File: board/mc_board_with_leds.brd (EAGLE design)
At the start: 70.3 x 34.5 mm, 36 parts, among them IC1 TPS61070DDC, IC2 MEGA8-P, Q2 16MHz

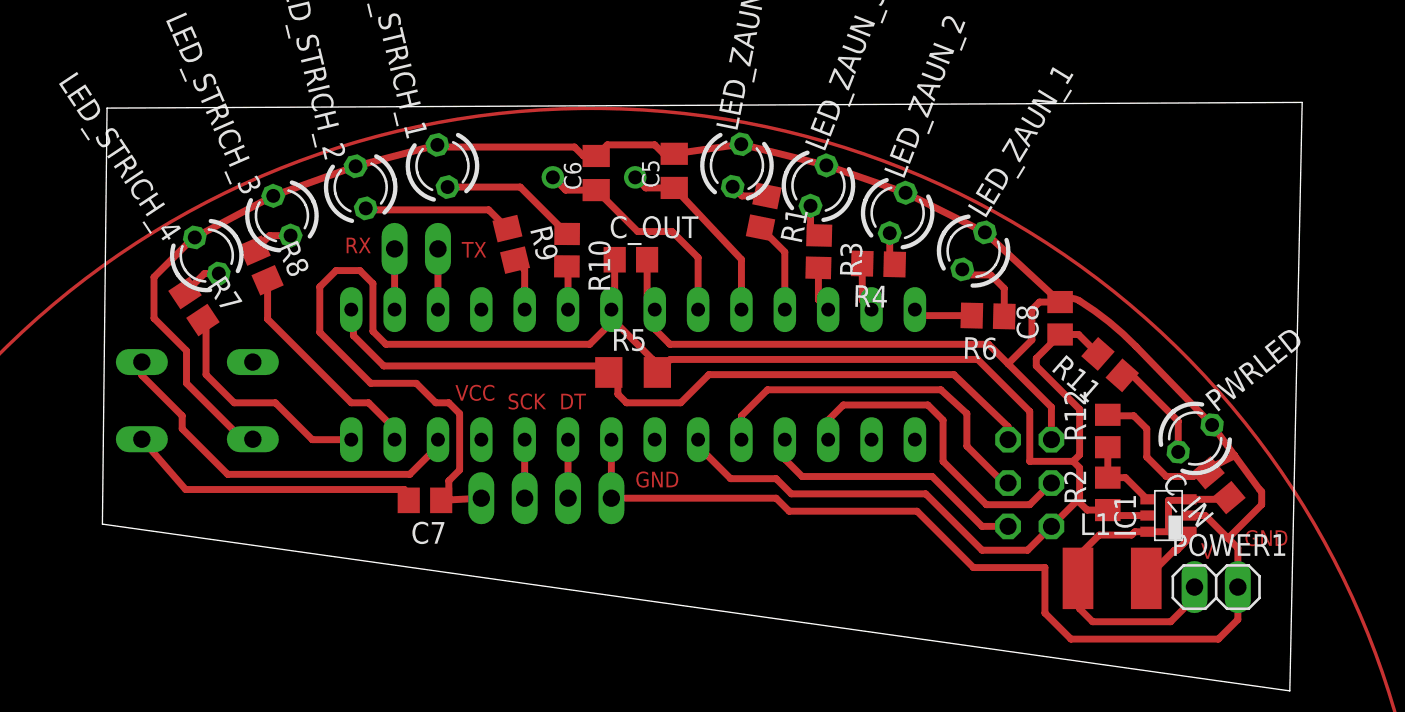
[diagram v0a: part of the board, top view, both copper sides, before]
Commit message: added drill holes
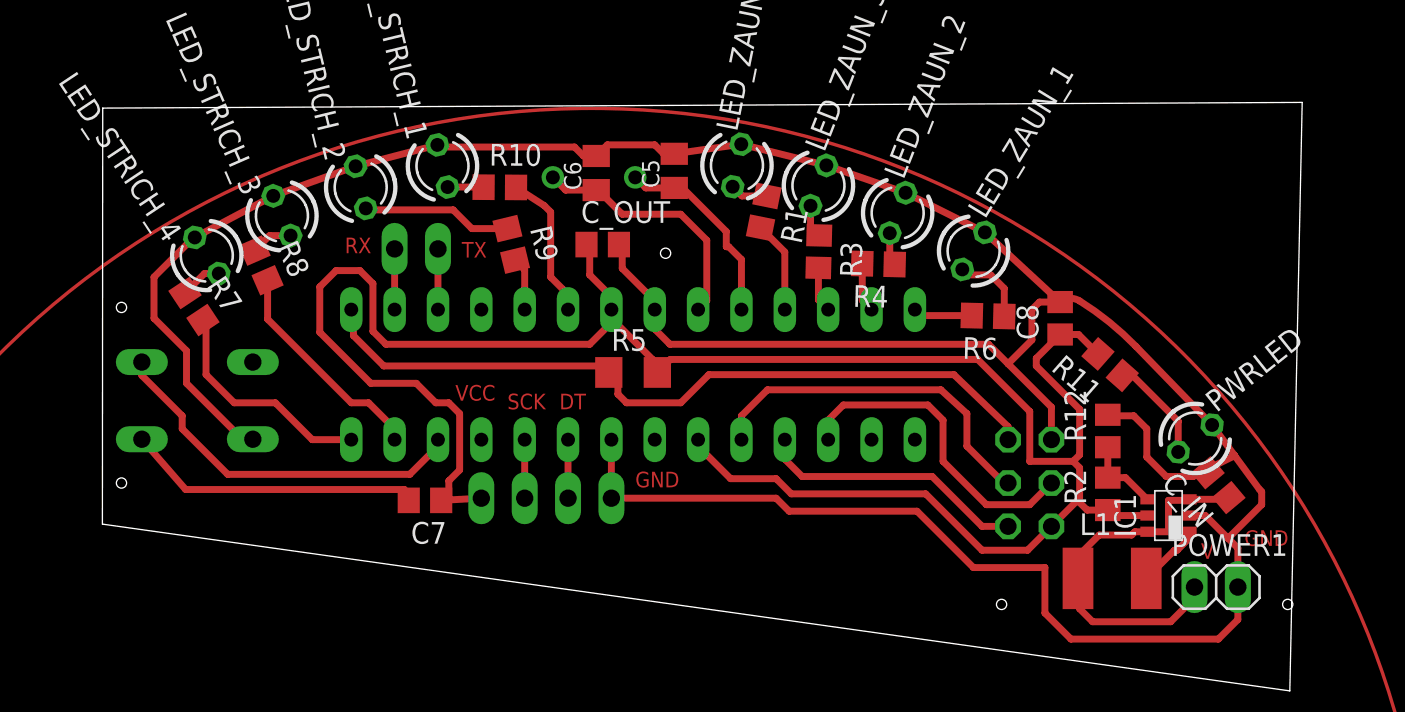
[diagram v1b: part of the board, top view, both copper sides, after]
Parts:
- moved R10 5.39 mm to (43.6, 44.4), turned to 359.6 degrees
- moved C_OUT 1.88 mm to (49.7, 41.0)
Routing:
- net PD4/LED_STRICH_1: track 2.56 -> 8.64 mm
- net N$12: track 8.14 -> 2.12 mm
- net GND: track 192.3 -> 193.9 mm
- net +5V: track 124.4 -> 125.8 mm
- net N$14: track 13.5 -> 14.8 mm
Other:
- outline, holes or cut-outs redrawn
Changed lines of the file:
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@@
 <layer number="43" name="vRestrict" color="2" fill="10" visible="no" active="yes"/>
 <layer number="44" name="Drills" color="7" fill="1" visible="no" active="yes"/>
-<layer number="45" name="Holes" color="7" fill="1" visible="no" active="yes"/>
+<layer number="45" name="Holes" color="7" fill="1" visible="yes" active="yes"/>
 <layer number="46" name="Milling" color="3" fill="1" visible="no" active="yes"/>
 <layer number="47" name="Measures" color="7" fill="1" visible="no" active="yes"/>
@@
 <board>
 <plain>
-<wire x1="20.345471875" y1="24.64364375" x2="20.617596875" y2="49.016115625" width="0" layer="20"/>
-<wire x1="20.617596875" y1="49.016115625" x2="90.63675" y2="49.349575" width="0" layer="20"/>
+<wire x1="20.345471875" y1="24.64364375" x2="20.363596875" y2="49.016115625" width="0" layer="20"/>
+<wire x1="20.363596875" y1="49.016115625" x2="90.63675" y2="49.349575" width="0" layer="20"/>
 <wire x1="90.63675" y1="49.349575" x2="89.912409375" y2="14.87245" width="0" layer="20"/>
 <wire x1="89.912409375" y1="14.87245" x2="20.345471875" y2="24.64364375" width="0" layer="20"/>
@@
 <text x="44.069" y="31.369" size="0.9144" layer="1" font="vector" ratio="28">SCK</text>
 <text x="41.021" y="31.877" size="0.9144" layer="1" font="vector" ratio="28">VCC</text>
+<hole x="21.463" y="37.338" drill="0.6"/>
+<hole x="89.789" y="19.939" drill="0.6"/>
+<hole x="73.025" y="19.939" drill="0.6"/>
+<hole x="21.463" y="27.051" drill="0.6"/>
+<hole x="53.34" y="40.513" drill="0.6"/>
 </plain>
 <attributes>
@@
 <element name="R8" library="resistor" package="R0805" value="470" x="29.6424875" y="39.798434375" rot="R293.6"/>
 <element name="R9" library="resistor" package="R0805" value="470" x="44.297534375" y="41.033296875" rot="R283.6"/>
-<element name="R10" library="resistor" package="R0805" value="470" x="47.565540625" y="40.692409375" rot="R269.6"/>
+<element name="R10" library="resistor" package="R0805" value="470" x="43.628540625" y="44.375409375" rot="R359.6"/>
 <element name="R11" library="resistor" package="R0805" value="470" x="79.383846875" y="33.986165625" rot="R138.6"/>
 <element name="PWRLED" library="led" package="LED3MM" value="" x="84.36773125" y="29.6607875" rot="R38.6"/>
@@
 <element name="R12" library="resistor" package="R0805" value="" x="79.248" y="30.099" rot="R90"/>
 <element name="C_IN" library="rcl-2" package="C0805" value="" x="85.725" y="26.924" rot="R130"/>
-<element name="C_OUT" library="rcl-2" package="C0805" value="" x="51.308" y="40.132"/>
+<element name="C_OUT" library="rcl-2" package="C0805" value="" x="49.657" y="41.021"/>
 </elements>
 <signals>
@@
 <wire x1="62.759478125" y1="45.658896875" x2="67.3998625" y2="44.054896875" width="0.4064" layer="1"/>
 <wire x1="67.3998625" y1="44.054896875" x2="72.04778125" y2="41.733921875" width="0.4064" layer="1"/>
-<wire x1="52.258" y1="40.132" x2="52.258" y2="37.658" width="0.4064" layer="1"/>
-<wire x1="52.258" y1="37.658" x2="52.705" y2="37.211" width="0.4064" layer="1"/>
 <wire x1="50.165" y1="26.162" x2="50.165" y2="29.591" width="0.4064" layer="1"/>
 <wire x1="76.454" y1="37.653" x2="72.04778125" y2="41.733921875" width="0.4064" layer="1"/>
@@
 <wire x1="88.265" y1="26.543" x2="88.265" y2="25.781" width="0.4064" layer="1"/>
 <wire x1="88.265" y1="25.781" x2="86.2965" y2="23.8125" width="0.4064" layer="1"/>
+<wire x1="52.705" y1="37.211" x2="52.705" y2="37.719" width="0.4064" layer="1"/>
+<wire x1="52.705" y1="37.719" x2="50.8" y2="39.624" width="0.4064" layer="1"/>
+<wire x1="50.8" y1="39.624" x2="50.8" y2="40.828" width="0.4064" layer="1"/>
+<wire x1="50.8" y1="40.828" x2="50.607" y2="41.021" width="0.4064" layer="1"/>
 </signal>
 <signal name="+5V">
@@
 <contactref element="R2" pad="1"/>
 <contactref element="C_OUT" pad="1"/>
-<wire x1="50.358" y1="40.132" x2="50.358" y2="37.404" width="0.4064" layer="1"/>
-<wire x1="50.358" y1="37.404" x2="50.165" y2="37.211" width="0.4064" layer="1"/>
 <wire x1="33.081" y1="38.542" x2="33.081" y2="35.88" width="0.4064" layer="1"/>
 <wire x1="33.081" y1="35.88" x2="36.068" y2="32.893" width="0.4064" layer="1"/>
@@
 <wire x1="52.578" y1="34.29" x2="52.578" y2="33.807" width="0.4064" layer="1"/>
 <wire x1="52.578" y1="33.807" x2="52.857" y2="33.528" width="0.4064" layer="1"/>
+<wire x1="50.165" y1="37.211" x2="50.165" y2="37.973" width="0.4064" layer="1"/>
+<wire x1="50.165" y1="37.973" x2="48.895" y2="39.243" width="0.4064" layer="1"/>
+<wire x1="48.895" y1="39.243" x2="48.895" y2="40.833" width="0.4064" layer="1"/>
+<wire x1="48.895" y1="40.833" x2="48.707" y2="41.021" width="0.4064" layer="1"/>
 </signal>
 <signal name="PB4/MISO">
@@
 <contactref element="IC2" pad="6"/>
 <contactref element="R10" pad="2"/>
-<wire x1="47.625" y1="37.211" x2="47.625" y2="39.6763375" width="0.4064" layer="1"/>
-<wire x1="47.625" y1="39.6763375" x2="47.55890625" y2="39.74243125" width="0.4064" layer="1" curve="90"/>
+<wire x1="44.578515625" y1="44.368775" x2="46.228" y2="43.307" width="0.4064" layer="1"/>
+<wire x1="47.625" y1="37.211" x2="47.371" y2="37.465" width="0.4064" layer="1"/>
+<wire x1="47.371" y1="37.465" x2="47.371" y2="38.354" width="0.4064" layer="1"/>
+<wire x1="47.371" y1="38.354" x2="46.609" y2="39.116" width="0.4064" layer="1"/>
+<wire x1="46.609" y1="39.116" x2="46.609" y2="42.926" width="0.4064" layer="1"/>
+<wire x1="46.609" y1="42.926" x2="46.228" y2="43.307" width="0.4064" layer="1"/>
 </signal>
 <signal name="PC0/DT">
@@
 <contactref element="LED_STRICH_2" pad="A"/>
 <wire x1="35.775934375" y1="43.140675" x2="35.863609375" y2="43.053" width="0.4064" layer="1"/>
-<wire x1="35.863609375" y1="43.053" x2="42.97780625" y2="43.053" width="0.4064" layer="1"/>
-<wire x1="44.074146875" y1="41.956659375" x2="42.97780625" y2="43.053" width="0.4064" layer="1"/>
+<wire x1="35.863609375" y1="43.053" x2="40.894" y2="43.053" width="0.4064" layer="1"/>
+<wire x1="40.894" y1="43.053" x2="41.990340625" y2="41.956659375" width="0.4064" layer="1"/>
+<wire x1="41.990340625" y1="41.956659375" x2="44.074146875" y2="41.956659375" width="0.4064" layer="1"/>
 </signal>
 <signal name="N$12">
 <contactref element="R10" pad="1"/>
 <contactref element="LED_STRICH_1" pad="A"/>
-<wire x1="47.572171875" y1="41.642384375" x2="44.8237125" y2="44.39084375" width="0.4064" layer="1"/>
-<wire x1="44.8237125" y1="44.39084375" x2="40.567609375" y2="44.39084375" width="0.4064" layer="1"/>
+<wire x1="40.567609375" y1="44.39084375" x2="42.6785625" y2="44.39084375" width="0.4064" layer="1"/>
+<wire x1="42.6785625" y1="44.39084375" x2="42.6785625" y2="44.382040625" width="0.4064" layer="1"/>
 </signal>
 <signal name="N$13">
@@
 <contactref element="IC2" pad="10"/>
 <wire x1="57.785" y1="37.211" x2="57.785" y2="40.148" width="0.4064" layer="1"/>
-<wire x1="57.785" y1="40.148" x2="53.848" y2="44.339" width="0.4064" layer="1"/>
 <wire x1="51.562" y1="44.958" x2="52.181" y2="44.339" width="0.4064" layer="1"/>
 <wire x1="52.181" y1="44.339" x2="53.848" y2="44.339" width="0.4064" layer="1"/>
+<wire x1="56.896" y1="40.894" x2="56.896" y2="41.783" width="0.4064" layer="1"/>
+<wire x1="56.896" y1="41.783" x2="54.34" y2="44.339" width="0.4064" layer="1"/>
+<wire x1="54.34" y1="44.339" x2="53.848" y2="44.339" width="0.4064" layer="1"/>
+<wire x1="57.785" y1="40.148" x2="57.039" y2="40.894" width="0.4064" layer="1"/>
+<wire x1="57.039" y1="40.894" x2="56.896" y2="40.894" width="0.4064" layer="1"/>
 </signal>
 <signal name="N$14">
@@
 <contactref element="Q2" pad="1"/>
 <contactref element="IC2" pad="9"/>
-<wire x1="51.705" y1="41.783" x2="53.721" y2="41.783" width="0.4064" layer="1"/>
-<wire x1="53.721" y1="41.783" x2="55.245" y2="40.259" width="0.4064" layer="1"/>
-<wire x1="55.245" y1="40.259" x2="55.245" y2="37.211" width="0.4064" layer="1"/>
 <wire x1="46.736" y1="44.958" x2="47.482" y2="44.212" width="0.4064" layer="1"/>
 <wire x1="47.482" y1="44.212" x2="49.276" y2="44.212" width="0.4064" layer="1"/>
-<wire x1="51.705" y1="41.783" x2="49.276" y2="44.212" width="0.4064" layer="1"/>
+<wire x1="55.245" y1="37.211" x2="55.753" y2="37.719" width="0.4064" layer="1"/>
+<wire x1="55.753" y1="37.719" x2="55.753" y2="41.275" width="0.4064" layer="1"/>
+<wire x1="55.753" y1="41.275" x2="54.229" y2="42.799" width="0.4064" layer="1"/>
+<wire x1="54.229" y1="42.799" x2="50.8" y2="42.799" width="0.4064" layer="1"/>
+<wire x1="50.8" y1="42.799" x2="49.387" y2="44.212" width="0.4064" layer="1"/>
+<wire x1="49.387" y1="44.212" x2="49.276" y2="44.212" width="0.4064" layer="1"/>
 </signal>
 <signal name="N$15">

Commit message: added ground fill
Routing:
- added copper zone on layer 1, net GND
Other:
- board size 70.3 x 34.5 mm -> 76.4 x 34.3 mm
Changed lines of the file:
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@@
 <board>
 <plain>
-<wire x1="20.345471875" y1="24.64364375" x2="20.363596875" y2="49.016115625" width="0" layer="20"/>
-<wire x1="20.363596875" y1="49.016115625" x2="90.63675" y2="49.349575" width="0" layer="20"/>
-<wire x1="90.63675" y1="49.349575" x2="89.912409375" y2="14.87245" width="0" layer="20"/>
-<wire x1="89.912409375" y1="14.87245" x2="20.345471875" y2="24.64364375" width="0" layer="20"/>
-<circle x="49" y="0" radius="49" width="0.2" layer="1"/>
+<wire x1="17.551471875" y1="15.11864375" x2="17.569596875" y2="49.270115625" width="0" layer="20"/>
+<wire x1="17.569596875" y1="49.270115625" x2="93.93875" y2="49.095575" width="0" layer="20"/>
+<wire x1="93.93875" y1="49.095575" x2="93.976409375" y2="14.99945" width="0" layer="20"/>
+<wire x1="93.976409375" y1="14.99945" x2="17.551471875" y2="15.11864375" width="0" layer="20"/>
+<circle x="49" y="0" radius="49" width="0.4" layer="1"/>
 <text x="34.544" y="40.513" size="0.9144" layer="1" font="vector" ratio="28">RX</text>
 <text x="41.402" y="40.259" size="0.9144" layer="1" font="vector" ratio="28">TX</text>
@@
 <text x="44.069" y="31.369" size="0.9144" layer="1" font="vector" ratio="28">SCK</text>
 <text x="41.021" y="31.877" size="0.9144" layer="1" font="vector" ratio="28">VCC</text>
-<hole x="21.463" y="37.338" drill="0.6"/>
-<hole x="89.789" y="19.939" drill="0.6"/>
-<hole x="73.025" y="19.939" drill="0.6"/>
-<hole x="21.463" y="27.051" drill="0.6"/>
-<hole x="53.34" y="40.513" drill="0.6"/>
+<hole x="21.463" y="37.338" drill="1.5"/>
+<hole x="89.789" y="19.939" drill="1.5"/>
+<hole x="73.025" y="19.939" drill="1.5"/>
+<hole x="21.463" y="27.051" drill="1.5"/>
+<hole x="53.34" y="40.513" drill="1.5"/>
 </plain>
 <attributes>
@@
 <contactref element="R12" pad="2"/>
 <wire x1="28.5496" y1="29.6164" x2="25.273" y2="32.893" width="0.4064" layer="1"/>
-<wire x1="49.276" y1="46.212" x2="49.927" y2="46.863" width="0.4064" layer="1"/>
-<wire x1="49.927" y1="46.863" x2="52.705" y2="46.863" width="0.4064" layer="1"/>
-<wire x1="52.705" y1="46.863" x2="53.229" y2="46.339" width="0.4064" layer="1"/>
+<wire x1="49.276" y1="46.212" x2="49.927" y2="46.482" width="0.4064" layer="1"/>
+<wire x1="49.927" y1="46.482" x2="52.705" y2="46.482" width="0.4064" layer="1"/>
+<wire x1="52.705" y1="46.482" x2="53.229" y2="46.339" width="0.4064" layer="1"/>
 <wire x1="53.229" y1="46.339" x2="53.848" y2="46.339" width="0.4064" layer="1"/>
 <wire x1="39.97035" y1="46.859621875" x2="40.093971875" y2="46.736" width="0.4064" layer="1"/>
@@
 <wire x1="50.8" y1="39.624" x2="50.8" y2="40.828" width="0.4064" layer="1"/>
 <wire x1="50.8" y1="40.828" x2="50.607" y2="41.021" width="0.4064" layer="1"/>
+<polygon width="0.4064" layer="1" isolate="0.6096">
+<vertex x="68.072" y="23.622"/>
+<vertex x="18.669" y="23.622"/>
+<vertex x="18.669" y="38.227"/>
+<vertex x="23.876" y="42.037"/>
+<vertex x="31.369" y="45.593"/>
+<vertex x="39.878" y="48.006"/>
+<vertex x="46.609" y="48.768"/>
+<vertex x="53.848" y="48.514"/>
+<vertex x="59.436" y="47.625"/>
+<vertex x="66.802" y="45.466"/>
+<vertex x="73.406" y="42.291"/>
+<vertex x="79.375" y="38.227"/>
+<vertex x="83.82" y="34.163"/>
+<vertex x="88.011" y="29.591"/>
+<vertex x="91.44" y="24.511"/>
+<vertex x="93.345" y="20.701"/>
+<vertex x="93.345" y="16.383"/>
+<vertex x="68.961" y="16.383"/>
+<vertex x="68.58" y="16.383"/>
+<vertex x="68.58" y="23.622"/>
+</polygon>
 </signal>
 <signal name="+5V">
